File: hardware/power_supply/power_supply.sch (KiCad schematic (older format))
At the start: 9 parts

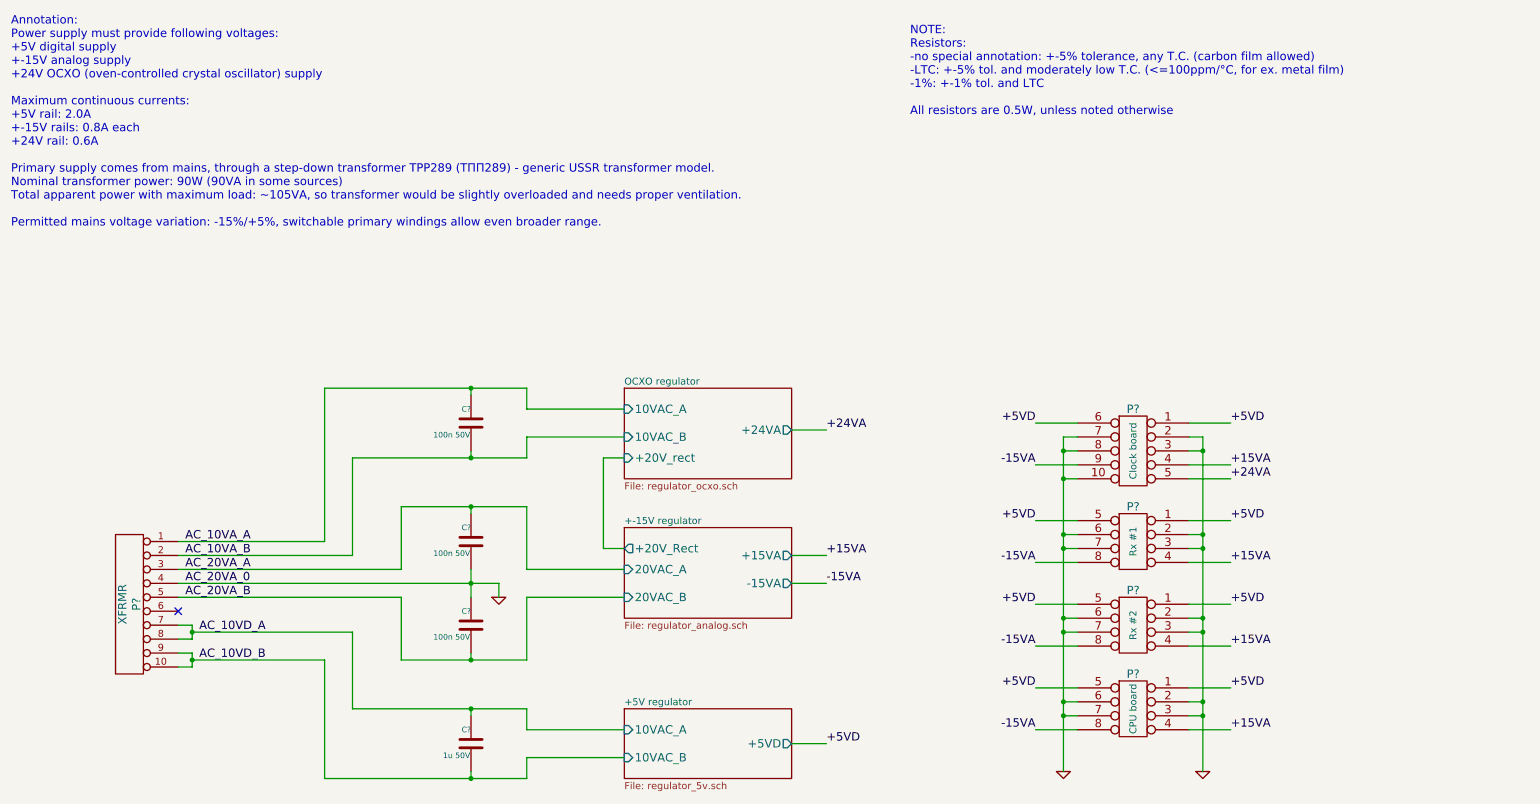
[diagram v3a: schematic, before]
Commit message: Update: PCB, schematic fixes -Almost completed power supply PCB -Removed discharge resistors from +-15, +24V supplies: no place on PCB for them -Removed ceramic capacitors (stayed in parallel with electrolytic caps): no reason for them
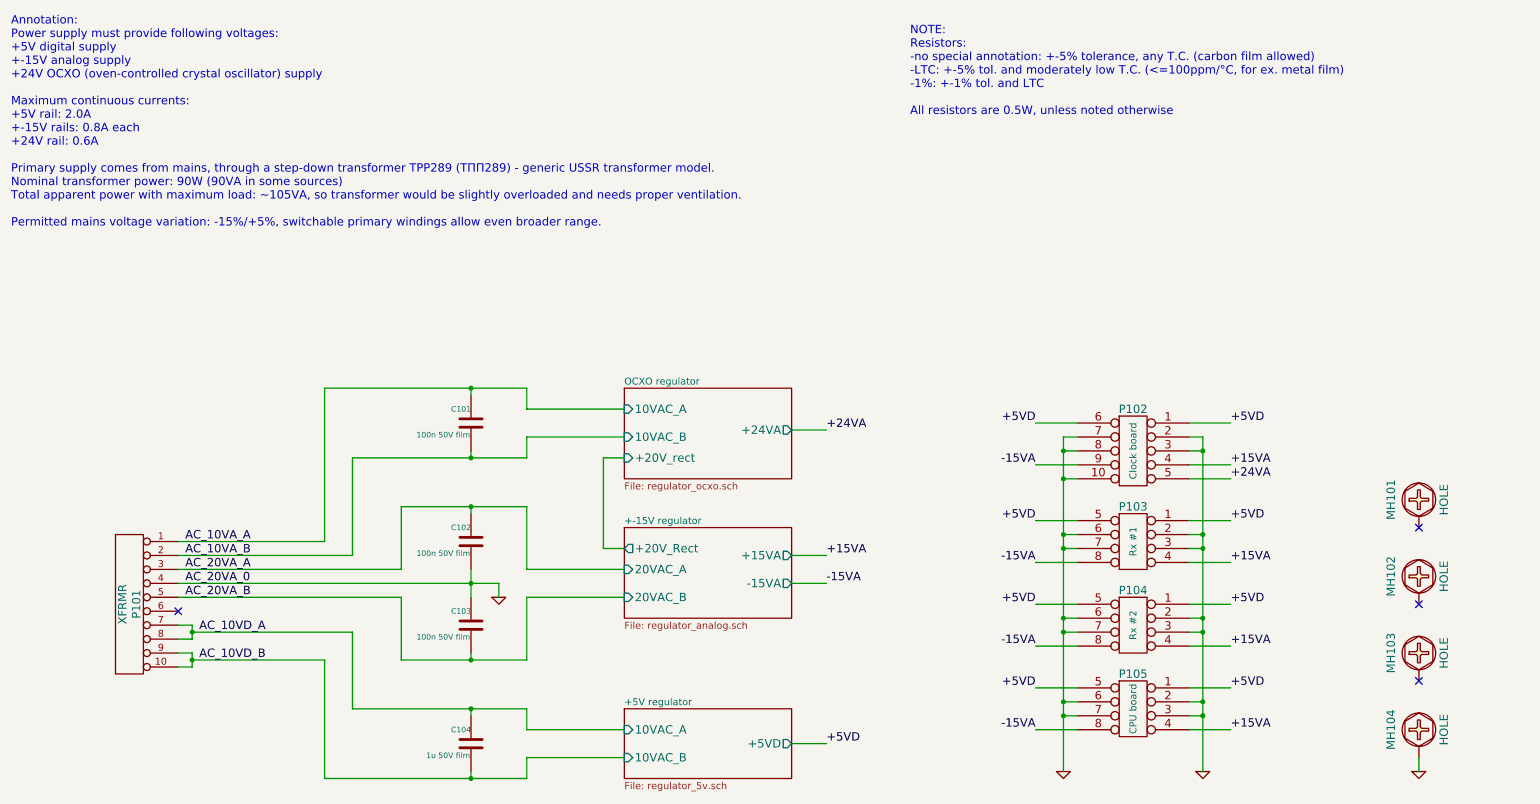
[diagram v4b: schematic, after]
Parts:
- added MH101, MH102, MH103, MH104: HOLE, symbol HOLE
- C101, C102, C103: renamed from C?; value 100n 50V -> 100n 50V film
- C104: renamed from C?; value 1u 50V -> 1u 50V film
- gave numbers to parts that had none: 5
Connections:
- net GND: now also MH104.1
- no-connect marks 1 -> 4
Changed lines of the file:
@@
 LIBS:scr
 LIBS:conn_mf
+LIBS:hole
 LIBS:power_supply-cache
 EELAYER 24 0
@@
 Annotation:\nPower supply must provide following voltages:\n+5V digital supply\n+-15V analog supply\n+24V OCXO (oven-controlled crystal oscillator) supply\n\nMaximum continuous currents:\n+5V rail: 2.0A \n+-15V rails: 0.8A each\n+24V rail: 0.6A\n\nPrimary supply comes from mains, through a step-down transformer TPP289 (ТПП289) - generic USSR transformer model.\nNominal transformer power: 90W (90VA in some sources)\nTotal apparent power with maximum load: ~~105VA, so transformer would be slightly overloaded and needs proper ventilation.\n\nPermitted mains voltage variation: -15%/+5%, switchable primary windings allow even broader range.
 $Comp
-L CONN_10 P?
+L CONN_10 P101
 U 1 1 5317B23A
 P 1500 4850
-F 0 "P?" V 1450 4850 60  0000 C CNN
+F 0 "P101" V 1450 4850 60  0000 C CNN
 F 1 "XFRMR" V 1550 4850 60  0000 C CNN
 F 2 "" H 1500 4850 60  0000 C CNN
@@
 NoConn ~ 1850 4900
 $Comp
-L GND #PWR?
+L GND #PWR01
 U 1 1 5317B345
 P 4150 4800
-F 0 "#PWR?" H 4150 4800 30  0001 C CNN
+F 0 "#PWR01" H 4150 4800 30  0001 C CNN
 F 1 "GND" H 4150 4730 30  0001 C CNN
 F 2 "" H 4150 4800 60  0000 C CNN
@@
 	1950 5100 1850 5100
 Wire Wire Line
-	1950 5000 1950 5050
-Wire Wire Line
-	1950 5050 1950 5100
+	1950 5000 1950 5100
 Wire Wire Line
 	1950 5000 1850 5000
@@
 	1850 5200 1950 5200
 Wire Wire Line
-	1950 5200 1950 5250
-Wire Wire Line
-	1950 5250 1950 5300
+	1950 5200 1950 5300
 Wire Wire Line
 	1950 5300 1850 5300
@@
 	1850 4800 3450 4800
 Wire Wire Line
-	1850 4700 3950 4700
-Wire Wire Line
-	3950 4700 4150 4700
+	1850 4700 4150 4700
 Wire Wire Line
 	1850 4600 3450 4600
@@
 $EndSheet
 $Comp
-L MF_8 P?
+L MF_8 P105
 U 1 1 5325450A
 P 8700 5600
-F 0 "P?" H 8700 5850 60  0000 C CNN
+F 0 "P105" H 8700 5850 60  0000 C CNN
 F 1 "CPU board" V 8700 5600 50  0000 C CNN
 F 2 "" H 8700 5400 60  0000 C CNN
@@
 $EndComp
 $Comp
-L MF_10 P?
+L MF_10 P102
 U 1 1 53254662
 P 8700 3750
-F 0 "P?" H 8700 4050 60  0000 C CNN
+F 0 "P102" H 8700 4050 60  0000 C CNN
 F 1 "Clock board" V 8700 3750 50  0000 C CNN
 F 2 "" H 8700 3600 60  0000 C CNN
@@
 $EndComp
 $Comp
-L MF_8 P?
+L MF_8 P104
 U 1 1 532548D2
 P 8700 5000
-F 0 "P?" H 8700 5250 60  0000 C CNN
+F 0 "P104" H 8700 5250 60  0000 C CNN
 F 1 "Rx #2" V 8700 5000 50  0000 C CNN
 F 2 "" H 8700 4800 60  0000 C CNN
@@
 $EndComp
 $Comp
-L MF_8 P?
+L MF_8 P103
 U 1 1 53254E50
 P 8700 4400
-F 0 "P?" H 8700 4650 60  0000 C CNN
+F 0 "P103" H 8700 4650 60  0000 C CNN
 F 1 "Rx #1" V 8700 4400 50  0000 C CNN
 F 2 "" H 8700 4200 60  0000 C CNN
@@
 +24VA
 Wire Wire Line
-	9200 3650 9200 3750
-Wire Wire Line
-	9200 3750 9200 4350
-Wire Wire Line
-	9200 4350 9200 4450
-Wire Wire Line
-	9200 4450 9200 4950
-Wire Wire Line
-	9200 4950 9200 5050
-Wire Wire Line
-	9200 5050 9200 5550
-Wire Wire Line
-	9200 5550 9200 5650
-Wire Wire Line
-	9200 5650 9200 6050
-Wire Wire Line
-	8200 3650 8200 3750
-Wire Wire Line
-	8200 3750 8200 3950
-Wire Wire Line
-	8200 3950 8200 4350
-Wire Wire Line
-	8200 4350 8200 4450
-Wire Wire Line
-	8200 4450 8200 4950
-Wire Wire Line
-	8200 4950 8200 5050
-Wire Wire Line
-	8200 5050 8200 5550
-Wire Wire Line
-	8200 5550 8200 5650
-Wire Wire Line
-	8200 5650 8200 6050
-$Comp
-L GND #PWR?
+	9200 3650 9200 6050
+Wire Wire Line
+	8200 3650 8200 6050
+$Comp
+L GND #PWR02
 U 1 1 53257FE8
 P 9200 6050
-F 0 "#PWR?" H 9200 6050 30  0001 C CNN
+F 0 "#PWR02" H 9200 6050 30  0001 C CNN
 F 1 "GND" H 9200 5980 30  0001 C CNN
 F 2 "" H 9200 6050 60  0000 C CNN
@@
 Connection ~ 8200 4350
 $Comp
-L GND #PWR?
+L GND #PWR03
 U 1 1 53258E8C
 P 8200 6050
-F 0 "#PWR?" H 8200 6050 30  0001 C CNN
+F 0 "#PWR03" H 8200 6050 30  0001 C CNN
 F 1 "GND" H 8200 5980 30  0001 C CNN
 F 2 "" H 8200 6050 60  0000 C CNN
@@
 	6250 3600 6500 3600
 $Comp
-L C C?
+L C C104
 U 1 1 5325C6D0
 P 3950 5850
-F 0 "C?" H 3950 5950 40  0000 L CNN
-F 1 "1u 50V" H 3956 5765 40  0000 L CNN
+F 0 "C104" H 3950 5950 40  0000 L CNN
+F 1 "1u 50V film" H 3956 5765 40  0000 L CNN
 F 2 "" H 3988 5700 30  0000 C CNN
 F 3 "" H 3950 5850 60  0000 C CNN
@@
 $EndComp
 $Comp
-L C C?
+L C C102
 U 1 1 5325C706
 P 3950 4400
-F 0 "C?" H 3950 4500 40  0000 L CNN
-F 1 "100n 50V" H 3956 4315 40  0000 L CNN
+F 0 "C102" H 3950 4500 40  0000 L CNN
+F 1 "100n 50V film" H 3956 4315 40  0000 L CNN
 F 2 "" H 3988 4250 30  0000 C CNN
 F 3 "" H 3950 4400 60  0000 C CNN
@@
 $EndComp
 $Comp
-L C C?
+L C C103
 U 1 1 5325C711
 P 3950 5000
-F 0 "C?" H 3950 5100 40  0000 L CNN
-F 1 "100n 50V" H 3956 4915 40  0000 L CNN
+F 0 "C103" H 3950 5100 40  0000 L CNN
+F 1 "100n 50V film" H 3956 4915 40  0000 L CNN
 F 2 "" H 3988 4850 30  0000 C CNN
 F 3 "" H 3950 5000 60  0000 C CNN
@@
 	4350 5750 4350 5600
 Wire Wire Line
-	4350 5600 3950 5600
-Wire Wire Line
-	3950 5600 3100 5600
+	4350 5600 3100 5600
 Wire Wire Line
 	3950 5600 3950 5650
@@
 	3950 6050 3950 6100
 Wire Wire Line
-	2900 6100 3950 6100
-Wire Wire Line
-	3950 6100 4350 6100
+	2900 6100 4350 6100
 Wire Wire Line
 	4350 6100 4350 5950
@@
 	3950 5200 3950 5250
 Wire Wire Line
-	3450 5250 3950 5250
-Wire Wire Line
-	3950 5250 4350 5250
+	3450 5250 4350 5250
 Wire Wire Line
 	4350 5250 4350 4800
@@
 	4350 4600 4350 4150
 Wire Wire Line
-	4350 4150 3950 4150
-Wire Wire Line
-	3950 4150 3450 4150
+	4350 4150 3450 4150
 Wire Wire Line
 	3950 4150 3950 4200
 $Comp
-L C C?
+L C C101
 U 1 1 5325CC3C
 P 3950 3550
-F 0 "C?" H 3950 3650 40  0000 L CNN
-F 1 "100n 50V" H 3956 3465 40  0000 L CNN
+F 0 "C101" H 3950 3650 40  0000 L CNN
+F 1 "100n 50V film" H 3956 3465 40  0000 L CNN
 F 2 "" H 3988 3400 30  0000 C CNN
 F 3 "" H 3950 3550 60  0000 C CNN
@@
 	4350 3450 4350 3300
 Wire Wire Line
-	4350 3300 3950 3300
-Wire Wire Line
-	3950 3300 2900 3300
+	4350 3300 2900 3300
 Wire Wire Line
 	3950 3300 3950 3350
@@
 	3950 3750 3950 3800
 Wire Wire Line
-	3100 3800 3950 3800
-Wire Wire Line
-	3950 3800 4350 3800
+	3100 3800 4350 3800
 Wire Wire Line
 	4350 3800 4350 3650
@@
 	4350 3650 5050 3650
 Wire Wire Line
-	3950 4600 3950 4700
-Wire Wire Line
-	3950 4700 3950 4800
+	3950 4600 3950 4800
 Connection ~ 3950 4700
 Wire Wire Line
@@
 	2900 5250 2900 6100
 Connection ~ 3950 6100
+$Comp
+L HOLE MH101
+U 1 1 532A1780
+P 10750 4100
+F 0 "MH101" H 10750 4300 60  0000 C CNN
+F 1 "HOLE" H 10750 3920 60  0000 C CNN
+F 2 "" H 10750 4100 60  0000 C CNN
+F 3 "" H 10750 4100 60  0000 C CNN
+	1    10750 4100
+	0    -1   -1   0
+$EndComp
+$Comp
+L HOLE MH102
+U 1 1 532A191E
+P 10750 4650
+F 0 "MH102" H 10750 4850 60  0000 C CNN
+F 1 "HOLE" H 10750 4470 60  0000 C CNN
+F 2 "" H 10750 4650 60  0000 C CNN
+F 3 "" H 10750 4650 60  0000 C CNN
+	1    10750 4650
+	0    -1   -1   0
+$EndComp
+$Comp
+L HOLE MH103
+U 1 1 532A1929
+P 10750 5200
+F 0 "MH103" H 10750 5400 60  0000 C CNN
+F 1 "HOLE" H 10750 5020 60  0000 C CNN
+F 2 "" H 10750 5200 60  0000 C CNN
+F 3 "" H 10750 5200 60  0000 C CNN
+	1    10750 5200
+	0    -1   -1   0
+$EndComp
+$Comp
+L HOLE MH104
+U 1 1 532A197C
+P 10750 5750
+F 0 "MH104" H 10750 5950 60  0000 C CNN
+F 1 "HOLE" H 10750 5570 60  0000 C CNN
+F 2 "" H 10750 5750 60  0000 C CNN
+F 3 "" H 10750 5750 60  0000 C CNN
+	1    10750 5750
+	0    -1   -1   0
+$EndComp
+$Comp
+L GND #PWR04
+U 1 1 532A1BE1
+P 10750 6050
+F 0 "#PWR04" H 10750 6050 30  0001 C CNN
+F 1 "GND" H 10750 5980 30  0001 C CNN
+F 2 "" H 10750 6050 60  0000 C CNN
+F 3 "" H 10750 6050 60  0000 C CNN
+	1    10750 6050
+	1    0    0    -1
+$EndComp
+Wire Wire Line
+	10750 5950 10750 6050
+NoConn ~ 10750 5400
+NoConn ~ 10750 4850
+NoConn ~ 10750 4300
 $EndSCHEMATC
